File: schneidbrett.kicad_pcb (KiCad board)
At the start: 4 copper layers, 132 parts, among them J1 USB_C_Receptacle, J2 Audio_Jack_Input, J3 Audio_Jack_Output, J4 UART_CONNECTOR, J5 JTAG 20-Pin, Q1 2N7002E, Q2 2N7002E, Q3 2N7002E, Q4 2N7002E, U1 MAX604, U2 AD9833xRM, U3 STM32F767ZITx, U4 LM4881M, U5 FT230XQ, Y1 Crystal

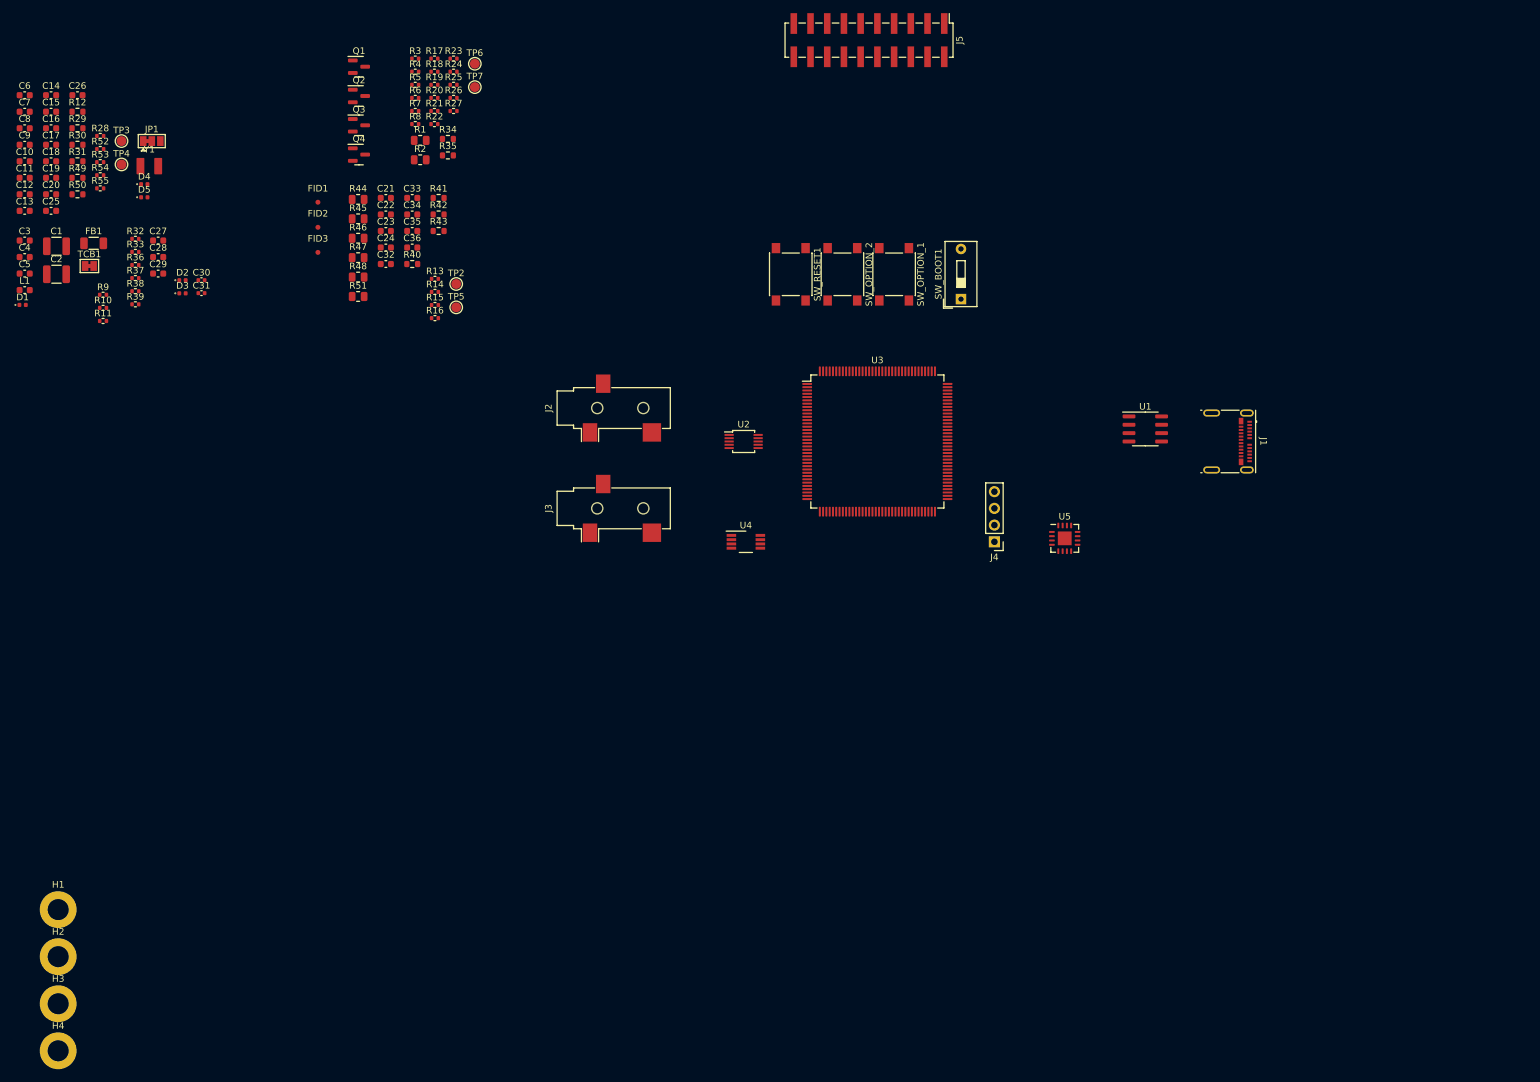
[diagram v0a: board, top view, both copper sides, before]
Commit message: Added ESD, updated Footprints, BOM, etc.
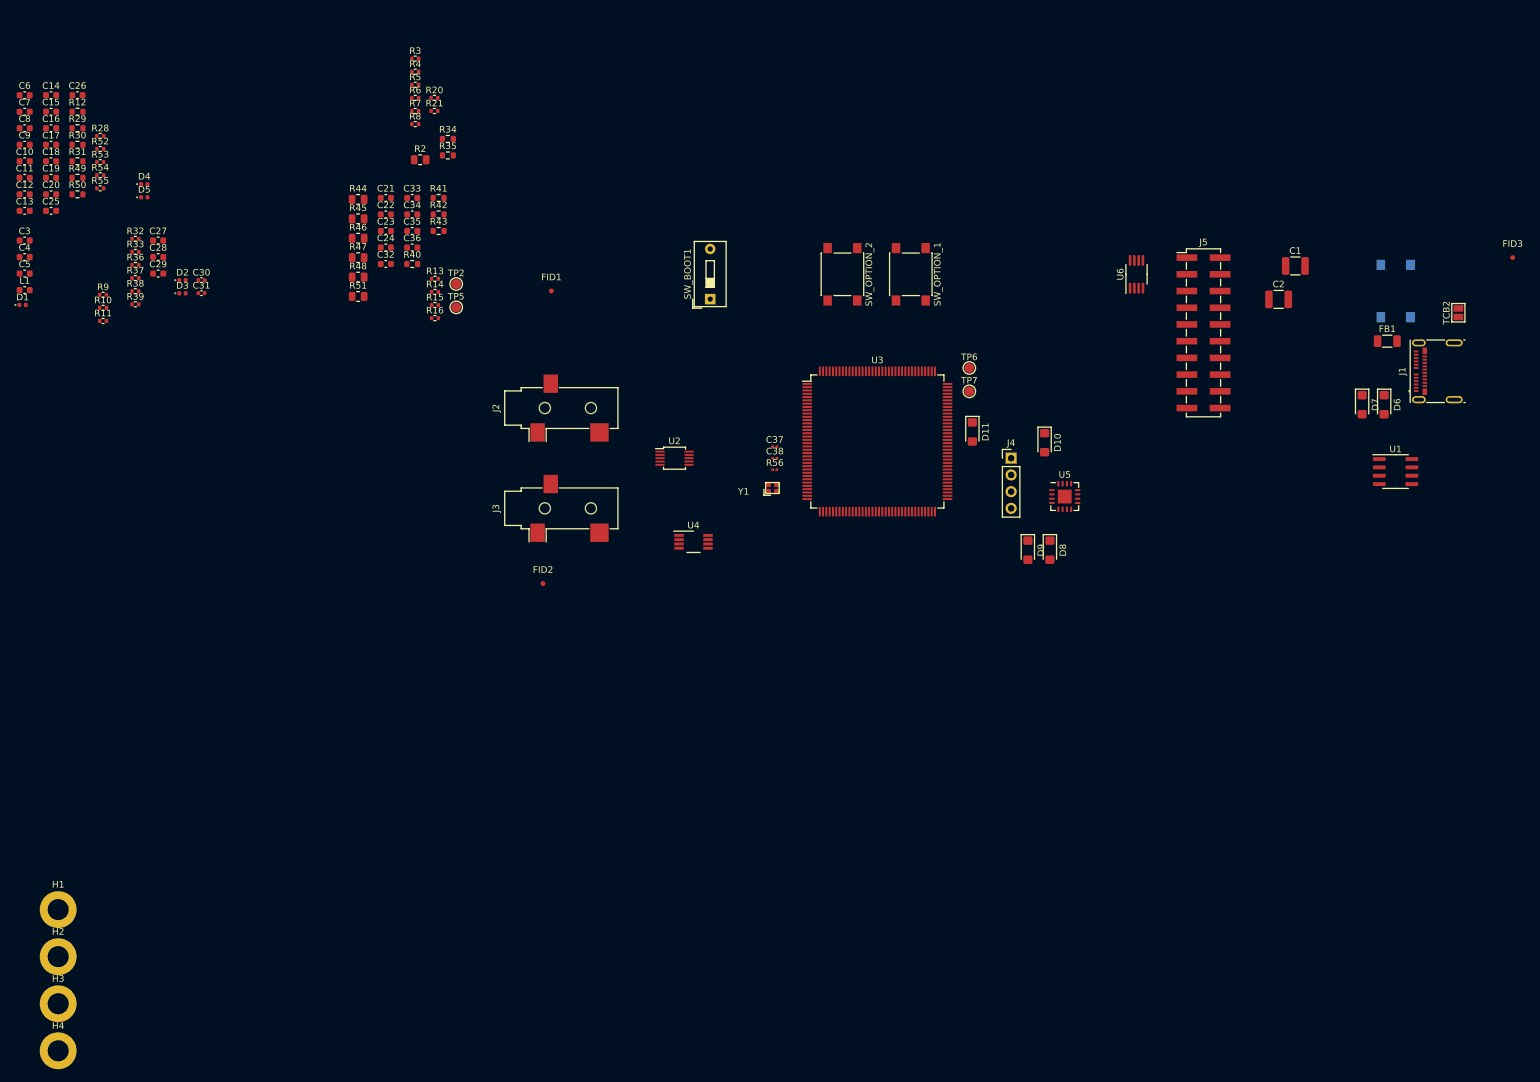
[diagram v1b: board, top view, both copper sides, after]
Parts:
- removed JP1: SolderJumper_3_Bridged, Jumper:SolderJumper-3_P1.3mm_Bridged12_Pad1.0x1.5mm
- removed Q1, Q2, Q3, Q4: 2N7002E, Package_TO_SOT_SMD:SOT-23
- removed R1: 0R, Resistor_SMD:R_0805_2012Metric
- removed R17, R18, R19: 4k7, Resistor_SMD:R_0402_1005Metric
- removed R22, R23, R24, R25, R26, R27: 0R, Resistor_SMD:R_0402_1005Metric
- removed TCB1: TEST_CON_BRIDGE, Jumper:SolderJumper-2_P1.3mm_Bridged_Pad1.0x1.5mm
- removed TP3: UART_RTS, TestPoint:TestPoint_Pad_D1.5mm
- removed TP4: UART_CTS, TestPoint:TestPoint_Pad_D1.5mm
- added C37: C, Capacitor_SMD:C_0201_0603Metric, F.Cu at (131.7, 94.8)
- added C38: C, Capacitor_SMD:C_0201_0603Metric, F.Cu at (131.7, 96.5)
- added D10: SMF5V0A, Diode_SMD:D_SMF, F.Cu at (172.7, 94.2)
- added D11: SMF5V0A, Diode_SMD:D_SMF, F.Cu at (161.8, 92.5)
- added D6: SMF5V0A, Diode_SMD:D_SMF, F.Cu at (224.3, 88.4)
- added D7: SMF5V0A, Diode_SMD:D_SMF, F.Cu at (221.0, 88.4)
- added D8: SMF5V0A, Diode_SMD:D_SMF, F.Cu at (173.5, 110.5)
- added D9: SMF5V0A, Diode_SMD:D_SMF, F.Cu at (170.2, 110.5)
- added R56: 0R, Resistor_SMD:R_0201_0603Metric, F.Cu at (131.7, 98.3)
- added TCB2: USB_SHIELDING_BRIDGE, Jumper:SolderJumper-2_P1.3mm_Open_Pad1.0x1.5mm, F.Cu at (235.6, 74.4)
- added U6: DT6250-06MR-13, Package_SO:MSOP-8_3x3mm_P0.65mm, F.Cu at (186.7, 68.6)
- C10, C11, C12, C13, C14, C15, C16, C17, C18, C19, C20, C21, C23, C27, C28, C4, C5, C7, C8, C9: value 0.1u -> 100n
- C32, C33, C34, C35: value 0.5u -> 500n
- D1: value PWRLED -> SML-LX0402UPGC-TR
- D2: value TXLED -> SML-LX0402SIC-TR
- D3: value RXLED -> SML-LX0402SOC-TR
- D4: value OPTION_LED_1 -> SML-LX0402USBC-TR
- D5: value OPTION_LED_2 -> SML-LX0402USBC-TR
- R40, R41, R42, R43: value 10 -> 10R
- SW_OPTION_1, SW_OPTION_2: value SW_Push -> PTS645SM43SMTR92 LFS
- SW_RESET1: value SW_Push -> PTS645SM43SMTR92 LFS; moved to B.Cu
- U1: value MAX604 -> MAX604CSA
- Y1: value Crystal -> CX2016SA25000F0FRZC1; footprint TimosFootprints:Crystal_SMD_MicroCrystal_CC6F_T1F_128 -> TimosFootprints:CX2016SA25000F0FRZC1
- moved FB1 197.1 mm to (224.8, 78.7)
- moved C1 188.2 mm to (210.8, 67.3)
- moved C2 185.7 mm to (208.3, 72.4)
- moved FID3 181.5 mm to (243.8, 66.0)
- moved Y1 106.6 mm to (131.4, 101.0)
- moved SW_RESET1 91.9 mm to (226.1, 71.1)
- moved TP6 88.2 mm to (161.3, 82.8)
- moved TP7 88.2 mm to (161.3, 86.4)
- moved J5 67.5 mm to (196.9, 77.5), turned to 0 degrees
- moved FID2 64.0 mm to (96.5, 115.6)
- moved U1 38.6 mm to (226.0, 98.5)
- moved SW_BOOT1 38.1 mm to (121.9, 72.3)
- moved FID1 37.9 mm to (97.8, 71.1)
- moved J1 33.5 mm to (232.4, 83.3), turned to 90 degrees
- moved J4 13.0 mm to (167.6, 96.5), turned to 0 degrees
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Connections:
- net Net-(D2-A) renamed /Peripherals/FTDI_LED1
- net Net-(D2-K) renamed /Peripherals/FTDI_CBUS1
- net Net-(D3-A) renamed /Peripherals/FTDI_LED2
- net Net-(D3-K) renamed /Peripherals/FTDI_CBUS2
- net Net-(D4-A) renamed /Controller/GPIO_LED_1_JUNCTION
- net Net-(D5-A) renamed /Controller/GPIO_LED_2_JUNCTION
- net Net-(J1-CC2) renamed /Connectors/USB_CC12
- net Net-(J5-~{SRST}) renamed /Connectors/JTAG_NSRST_INNER
- net Net-(J5-~{TRST}) renamed /Connectors/JTAG_NTRST_INNER
- net Net-(R44-Pad1) renamed /Analog/AUDIO_GND_STARPOINT
- net Net-(U1-SET) renamed /Power Supply/POWER_SET_TERMINAL
- net Net-(U2-CAP/2.5V) renamed /Analog/GEN_CAP
- net Net-(U2-COMP) renamed /Analog/GEN_COMP
- net Net-(U2-MCLK) renamed /Analog/GEN_MCLK
- net Net-(U3-BOOT0) renamed /Controller/MCU_BOOT0
- net Net-(U3-PDR_ON) renamed /Controller/MCU_PDR_ON
- net Net-(U3-VBAT) renamed /Controller/MCU_VBAT
- net Net-(U4-BYPASS) renamed /Analog/AUDIO_BYPASS
- net Net-(U4-VDD) renamed /Analog/AUDIO_PWR_JUNCTION
- J1 pad A5: Net-(J1-CC1) -> /Connectors/USB_CC1
- J1 pad S1: Net-(J1-SHIELD) -> /Connectors/USB_CC1
- J4 pad 3: unconnected-(J4-Pin_3-Pad3) -> MCU_UART_RX
- R20 pad 2: JTAG_TRST -> JTAG_NTRST
- R21 pad 2: JTAG_NRST -> JTAG_NSRST
- R30 pad 1: Net-(U3-VDDSDMMC) -> +3.3V
- R30 pad 2: +3.3V -> /Controller/MCU_VDDSDMMC
- R31 pad 1: Net-(U3-VDDUSB) -> +3.3V
- R31 pad 2: +3.3V -> /Controller/MCU_VDDUSB
- R35 pad 1: Net-(J1-CC1) -> /Connectors/USB_CC1
- SW_RESET1 pad 1: GLOBAL_NRESET -> JTAG_NSRST
- U3 pad 105: unconnected-(U3-PA13-Pad105) -> JTAG_TMS
- U3 pad 109: unconnected-(U3-PA14-Pad109) -> JTAG_TCK
- U3 pad 110: unconnected-(U3-PA15-Pad110) -> JTAG_TDI
- U3 pad 121: Net-(U3-VDDSDMMC) -> /Controller/MCU_VDDSDMMC
- U3 pad 125: unconnected-(U3-PG10-Pad125) -> GPIO_LED_2
- U3 pad 126: GEN_SPI_CLK -> GPIO_LED_1
- U3 pad 127: unconnected-(U3-PG12-Pad127) -> GPIO_BTN_2
- U3 pad 128: GEN_SPI_CSEL -> GPIO_BTN_1
- U3 pad 133: unconnected-(U3-PB3-Pad133) -> JTAG_TDO
- U3 pad 134: unconnected-(U3-PB4-Pad134) -> JTAG_NTRST
- U3 pad 135: GEN_SPI_DATA_MCU_1 -> unconnected-(U3-PB5-Pad135)
- U3 pad 23: CRYSTAL_PH0 -> MCU_CRYSTAL_PH0
- U3 pad 24: CRYSTAL_PH1 -> MCU_CRYSTAL_PH1
- U3 pad 25: GLOBAL_NRESET -> JTAG_NSRST
- U3 pad 27: unconnected-(U3-PC1-Pad27) -> GEN_SPI_DATA
- U3 pad 28: unconnected-(U3-PC2-Pad28) -> GEN_SPI_CSEL
- U3 pad 43: GEN_SPI_DATA_MCU_0 -> unconnected-(U3-PA7-Pad43)
- U3 pad 69: unconnected-(U3-PB10-Pad69) -> GEN_SPI_CLK
- U3 pad 87: GPIO_LED_2 -> unconnected-(U3-PG2-Pad87)
- U3 pad 88: GPIO_LED_1 -> unconnected-(U3-PG3-Pad88)
- U3 pad 89: GPIO_BTN_2 -> unconnected-(U3-PG4-Pad89)
- U3 pad 90: GPIO_BTN_1 -> unconnected-(U3-PG5-Pad90)
- U3 pad 95: Net-(U3-VDDUSB) -> /Controller/MCU_VDDUSB
- Y1 pad 1: unconnected-(Y1-Pad1) -> MCU_CRYSTAL_PH0
- Y1 pad 2: unconnected-(Y1-Pad2) -> GND

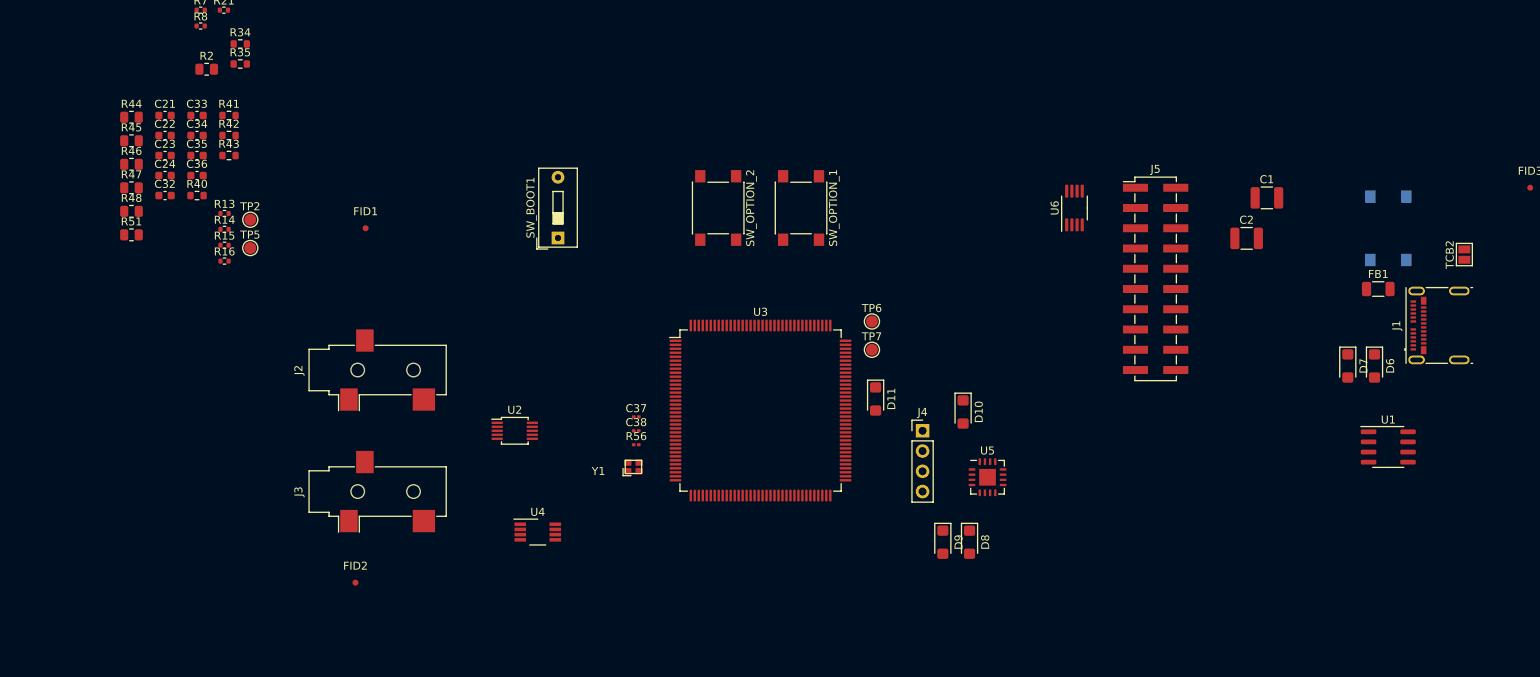
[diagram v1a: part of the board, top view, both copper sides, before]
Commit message: Schematic is done for now, starting layout
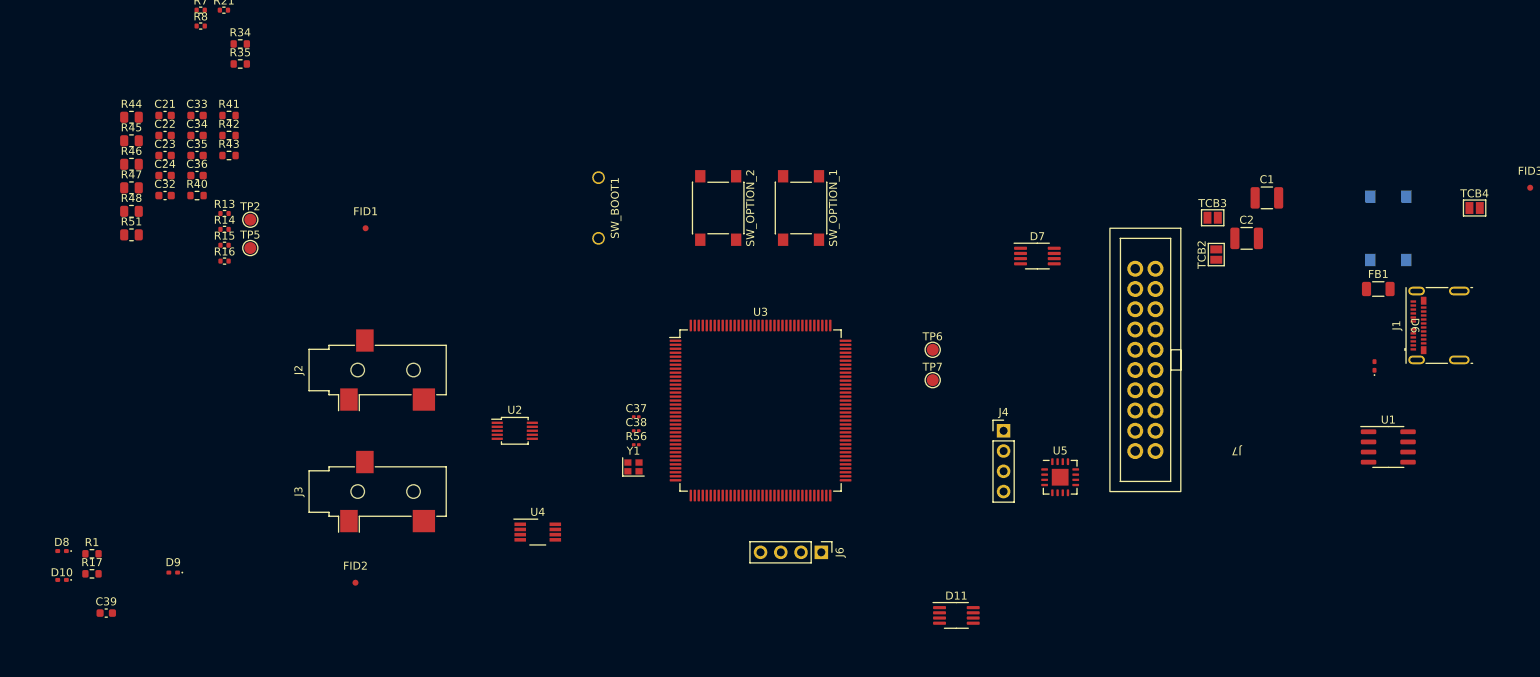
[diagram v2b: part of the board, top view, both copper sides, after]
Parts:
- removed J5: JTAG 20-Pin, Connector_PinHeader_2.54mm:PinHeader_2x10_P2.54mm_Vertical_SMD
- removed R2: 0R, Resistor_SMD:R_0805_2012Metric
- removed U6: DT6250-06MR-13, Package_SO:MSOP-8_3x3mm_P0.65mm
- added C39: 100n, Capacitor_SMD:C_0603_1608Metric, F.Cu at (65.3, 119.4)
- added J6: I2C_CONNECTOR, Connector_PinHeader_2.54mm:PinHeader_1x04_P2.54mm_Vertical, F.Cu at (154.9, 111.8)
- added J7: ST-LINK_V2_20Pin_Connector, TimosFootprints:ST-LINK_V2_20Pin_Connector, F.Cu at (195.6, 87.6)
- added R1: 5k1, Resistor_SMD:R_0603_1608Metric, F.Cu at (63.5, 112.0)
- added R17: 5k1, Resistor_SMD:R_0603_1608Metric, F.Cu at (63.5, 114.5)
- added TCB3: ~, Jumper:SolderJumper-2_P1.3mm_Open_Pad1.0x1.5mm, F.Cu at (204.0, 69.8)
- added TCB4: USB_SHIELDING_BRIDGE, Jumper:SolderJumper-2_P1.3mm_Open_Pad1.0x1.5mm, F.Cu at (236.9, 68.6)
- C25, C26: value 10u -> 2u2
- C37, C38: value C -> 10p
- D10, D6, D8, D9: value SMF5V0A -> TVSA04V05C006; footprint Diode_SMD:D_SMF -> TimosFootprints:TVSA04V05C006
- D11, D7: value SMF5V0A -> DT6250-06MR-13; footprint Diode_SMD:D_SMF -> Package_SO:MSOP-8_3x3mm_P0.65mm
- R28, R36, R37: value 10k -> 5k1
- R49, R50: value 0R -> 100R
- SW_BOOT1: footprint Button_Switch_THT:SW_DIP_SPSTx01_Slide_9.78x4.72mm_W7.62mm_P2.54mm -> TimosFootprints:DS01-254-L-01BE
- TCB2: value USB_SHIELDING_BRIDGE -> ~
- Y1: value CX2016SA25000F0FRZC1 -> 25MHz; footprint TimosFootprints:CX2016SA25000F0FRZC1 -> Crystal:Crystal_SMD_2016-4Pin_2.0x1.6mm
- moved D10 114.9 mm to (59.7, 115.2), turned to 0 degrees
- moved D8 113.8 mm to (59.7, 111.6), turned to 0 degrees
- moved D9 96.6 mm to (73.7, 114.3), turned to 0 degrees
- moved D7 41.3 mm to (182.0, 74.6), turned to 0 degrees
- moved TCB2 31.1 mm to (204.5, 74.4)
- moved D11 29.0 mm to (171.9, 119.7), turned to 0 degrees
- moved J4 10.2 mm to (177.8, 96.5)
- moved U5 9.11 mm to (184.9, 102.3)
- moved TP7 8.52 mm to (168.9, 90.2)
- moved TP6 8.41 mm to (168.9, 86.4)
- moved SW_BOOT1 6.32 mm to (127.0, 68.6)
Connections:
- net FTDI_USBDM renamed FTDI_USBD-
- net FTDI_USBDP renamed FTDI_USBD+
- C22 pad 2: GNDA -> GND
- C23 pad 2: GNDA -> GND
- C3 pad 2: GNDA -> GND
- C30 pad 1: USBP -> USB+
- C31 pad 1: USBM -> USB-
- C36 pad 2: GNDA -> GND
- C4 pad 2: GNDA -> GND
- D10 pad 1: MCU_UART_CTS -> GND
- D10 pad 2: GND -> USB+
- D11 pad 1: MCU_UART_RTS -> MCU_UART_CTS
- D11 pad 2: GND -> MCU_UART_RTS
- D6 pad 1: USBM -> GND
- D6 pad 2: GND -> USB-
- D7 pad 1: USBP -> /Connectors/JTAG_NTRST_INNER
- D7 pad 2: GND -> /Connectors/JTAG_NSRST_INNER
- D8 pad 1: MCU_UART_TX -> GND
- D8 pad 2: GND -> MCU_I2C_SCL
- D9 pad 1: MCU_UART_RX -> GND
- D9 pad 2: GND -> MCU_I2C_SDA
- J1 pad A6: USBP -> USB+
- J1 pad A7: USBM -> USB-
- J1 pad B6: USBP -> USB+
- J1 pad B7: USBM -> USB-
- R38 pad 2: USBP -> USB+
- R39 pad 2: USBM -> USB-
- R46 pad 2: GNDA -> GND
- TCB2 pad 1: /Connectors/USB_CC1 -> +3.3V
- TCB2 pad 2: GND -> Net-(J7-VAPP)
- U2 pad 9: GNDA -> GND
- U3 pad 31: GNDA -> GND
- U3 pad 54: unconnected-(U3-PF14-Pad54) -> MCU_I2C_SCL
- U3 pad 55: unconnected-(U3-PF15-Pad55) -> MCU_I2C_SDA
- U4 pad 2: GNDA -> GND
